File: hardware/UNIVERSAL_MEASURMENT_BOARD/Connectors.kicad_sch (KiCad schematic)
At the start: 44 parts, among them J1 2606-1110_010-000, J2 2606-1110_010-000, J3 2606-1110_010-000, J4 2606-1110_010-000, J5 Strain Relief, J6 Strain Relief, J7 FTSH-107-01-L-D-K, J8 Strain Relief, J9 Strain Relief

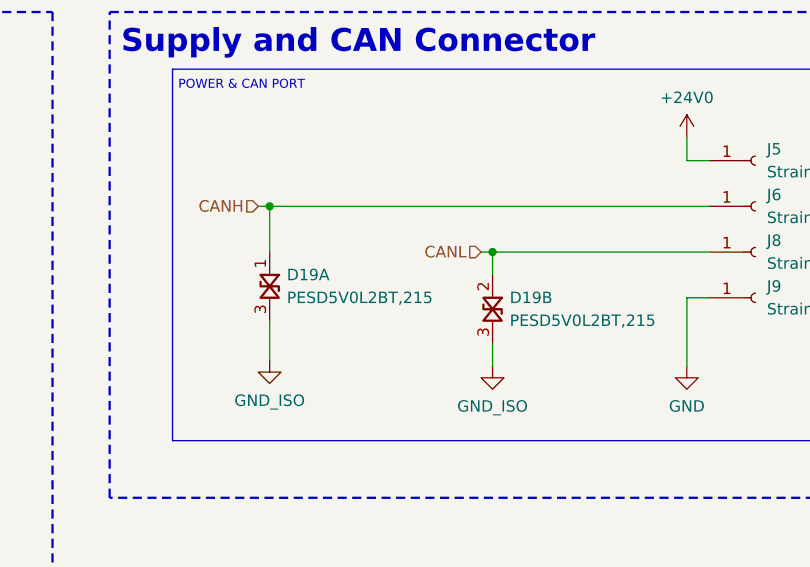
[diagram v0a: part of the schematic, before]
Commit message: Add CAN interface to PCB, continue work on power section
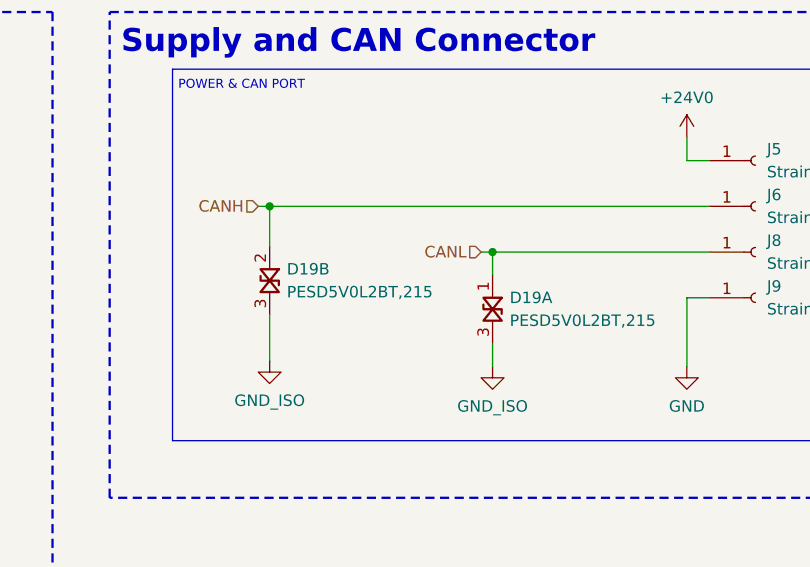
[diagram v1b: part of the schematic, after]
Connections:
- net CANH: now also D19.2; no longer D19.1
- net CANL: now also D19.1; no longer D19.2
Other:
- moved on the sheet: D19A, D19B
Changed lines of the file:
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@@
 	)
 	(junction
-		(at 194.31 181.61)
+		(at 241.935 120.65)
 		(diameter 0)
 		(color 0 0 0 0)
 	)
 	(junction
-		(at 241.935 120.65)
+		(at 309.88 73.66)
 		(diameter 0)
 		(color 0 0 0 0)
 	)
 	(junction
-		(at 309.88 73.66)
+		(at 169.545 176.53)
 		(diameter 0)
 		(color 0 0 0 0)
@@
 	)
 	(junction
-		(at 106.045 210.82)
+		(at 194.31 181.61)
 		(diameter 0)
 		(color 0 0 0 0)
 	)
 	(junction
-		(at 173.99 120.65)
+		(at 106.045 210.82)
 		(diameter 0)
 		(color 0 0 0 0)
 	)
 	(junction
-		(at 169.545 176.53)
+		(at 173.99 120.65)
 		(diameter 0)
 		(color 0 0 0 0)
@@
 	(wire
 		(pts
-			(xy 169.545 189.23) (xy 169.545 193.675)
-		)
-		(stroke
-			(width 0)
-			(type default)
-		)
-	)
-	(wire
-		(pts
 			(xy 116.205 58.42) (xy 121.285 58.42)
 		)
@@
 	(wire
 		(pts
-			(xy 193.04 181.61) (xy 194.31 181.61)
+			(xy 241.935 123.19) (xy 241.935 120.65)
 		)
 		(stroke
@@
 	(wire
 		(pts
-			(xy 241.935 123.19) (xy 241.935 120.65)
+			(xy 169.545 188.595) (xy 169.545 193.675)
 		)
 		(stroke
@@
 	(wire
 		(pts
+			(xy 169.545 176.53) (xy 169.545 180.975)
+		)
+		(stroke
+			(width 0)
+			(type default)
+		)
+	)
+	(wire
+		(pts
 			(xy 127.635 86.36) (xy 127.635 81.28)
 		)
@@
 	(wire
 		(pts
-			(xy 194.31 181.61) (xy 218.44 181.61)
+			(xy 193.04 181.61) (xy 194.31 181.61)
 		)
 		(stroke
@@
 	(wire
 		(pts
-			(xy 169.545 176.53) (xy 169.545 181.61)
-		)
-		(stroke
-			(width 0)
-			(type default)
-		)
-	)
-	(wire
-		(pts
 			(xy 173.99 102.87) (xy 173.99 111.125)
 		)
@@
 	(wire
 		(pts
-			(xy 194.31 191.77) (xy 194.31 194.31)
+			(xy 194.31 181.61) (xy 218.44 181.61)
 		)
 		(stroke
@@
 	(wire
 		(pts
+			(xy 194.31 191.77) (xy 194.31 194.31)
+		)
+		(stroke
+			(width 0)
+			(type default)
+		)
+	)
+	(wire
+		(pts
 			(xy 168.275 176.53) (xy 169.545 176.53)
 		)
@@
 	(wire
 		(pts
-			(xy 169.545 176.53) (xy 218.44 176.53)
-		)
-		(stroke
-			(width 0)
-			(type default)
-		)
-	)
-	(wire
-		(pts
 			(xy 330.2 58.42) (xy 334.01 58.42)
 		)
@@
 	(wire
 		(pts
-			(xy 194.31 181.61) (xy 194.31 184.15)
+			(xy 106.045 55.88) (xy 106.045 64.135)
 		)
 		(stroke
@@
 	(wire
 		(pts
-			(xy 106.045 55.88) (xy 106.045 64.135)
+			(xy 85.09 174.625) (xy 98.425 174.625)
 		)
 		(stroke
@@
 	(wire
 		(pts
-			(xy 85.09 174.625) (xy 98.425 174.625)
+			(xy 194.31 181.61) (xy 194.31 184.15)
 		)
 		(stroke
@@
 	(wire
 		(pts
+			(xy 169.545 176.53) (xy 218.44 176.53)
+		)
+		(stroke
+			(width 0)
+			(type default)
+		)
+	)
+	(wire
+		(pts
 			(xy 116.205 105.41) (xy 121.285 105.41)
 		)
@@
 	(symbol
 		(lib_id "PESD5V0L2BT,215:PESD5V0L2BT,215")
-		(at 169.545 185.42 270)
+		(at 194.31 187.96 270)
 		(unit 1)
 		(body_style 1)
@@
 		(fields_autoplaced yes)
 		(property "Reference" "D19"
-			(at 171.45 184.1499 90)
+			(at 196.215 186.6899 90)
 			(show_name no)
 			(do_not_autoplace no)
@@
 		)
 		(property "Value" "PESD5V0L2BT,215"
-			(at 171.45 186.6899 90)
+			(at 196.215 189.2299 90)
 			(show_name no)
 			(do_not_autoplace no)
@@
 		)
 		(property "Footprint" "SOT95P230X110-3N"
-			(at 89.865 212.09 0)
+			(at 114.63 214.63 0)
 			(hide yes)
 			(show_name no)
@@
 		)
 		(property "Datasheet" "https://assets.nexperia.com/documents/data-sheet/PESDXL2BT_SER.pdf"
-			(at -10.135 212.09 0)
+			(at 14.63 214.63 0)
 			(hide yes)
 			(show_name no)
@@
 		)
 		(property "Description" "Low capacitance double bidirectional ESD protection diodes in SOT23 13A 30kV"
-			(at 193.675 185.42 0)
+			(at 218.44 187.96 0)
 			(hide yes)
 			(show_name no)
@@
 		)
 		(property "Height" "1.1"
-			(at -210.135 212.09 0)
+			(at -185.37 214.63 0)
 			(hide yes)
 			(show_name no)
@@
 		)
 		(property "Mouser Part Number" "771-PESD5V0L2BT-T/R"
-			(at -310.135 212.09 0)
+			(at -285.37 214.63 0)
 			(hide yes)
 			(show_name no)
@@
 		)
 		(property "Mouser Price/Stock" "https://www.mouser.co.uk/ProductDetail/Nexperia/PESD5V0L2BT215?qs=LOCUfHb8d9sw%252B%2FcZzpNtzw%3D%3D"
-			(at -410.135 212.09 0)
+			(at -385.37 214.63 0)
 			(hide yes)
 			(show_name no)
@@
 		)
 		(property "Manufacturer_Name" "Nexperia"
-			(at -510.135 212.09 0)
+			(at -485.37 214.63 0)
 			(hide yes)
 			(show_name no)
@@
 		)
 		(property "Manufacturer_Part_Number" "PESD5V0L2BT,215"
-			(at -610.135 212.09 0)
+			(at -585.37 214.63 0)
 			(hide yes)
 			(show_name no)
@@
 	(symbol
 		(lib_id "PESD5V0L2BT,215:PESD5V0L2BT,215")
-		(at 194.31 187.96 270)
+		(at 169.545 184.785 270)
 		(unit 2)
 		(body_style 1)
@@
 		(fields_autoplaced yes)
 		(property "Reference" "D19"
-			(at 196.215 186.6899 90)
+			(at 171.45 183.5149 90)
 			(show_name no)
 			(do_not_autoplace no)
@@
 		)
 		(property "Value" "PESD5V0L2BT,215"
-			(at 196.215 189.2299 90)
+			(at 171.45 186.0549 90)
 			(show_name no)
 			(do_not_autoplace no)
@@
 		)
 		(property "Footprint" "SOT95P230X110-3N"
-			(at 114.63 214.63 0)
+			(at 89.865 211.455 0)
 			(hide yes)
 			(show_name no)
@@
 		)
 		(property "Datasheet" "https://assets.nexperia.com/documents/data-sheet/PESDXL2BT_SER.pdf"
-			(at 14.63 214.63 0)
+			(at -10.135 211.455 0)
 			(hide yes)
 			(show_name no)
@@
 		)
 		(property "Description" "Low capacitance double bidirectional ESD protection diodes in SOT23 13A 30kV"
-			(at 218.44 187.96 0)
+			(at 193.675 184.785 0)
 			(hide yes)
 			(show_name no)
@@
 		)
 		(property "Height" "1.1"
-			(at -185.37 214.63 0)
+			(at -210.135 211.455 0)
 			(hide yes)
 			(show_name no)
@@
 		)
 		(property "Mouser Part Number" "771-PESD5V0L2BT-T/R"
-			(at -285.37 214.63 0)
+			(at -310.135 211.455 0)
 			(hide yes)
 			(show_name no)
@@
 		)
 		(property "Mouser Price/Stock" "https://www.mouser.co.uk/ProductDetail/Nexperia/PESD5V0L2BT215?qs=LOCUfHb8d9sw%252B%2FcZzpNtzw%3D%3D"
-			(at -385.37 214.63 0)
+			(at -410.135 211.455 0)
 			(hide yes)
 			(show_name no)
@@
 		)
 		(property "Manufacturer_Name" "Nexperia"
-			(at -485.37 214.63 0)
+			(at -510.135 211.455 0)
 			(hide yes)
 			(show_name no)
@@
 		)
 		(property "Manufacturer_Part_Number" "PESD5V0L2BT,215"
-			(at -585.37 214.63 0)
+			(at -610.135 211.455 0)
 			(hide yes)
 			(show_name no)
